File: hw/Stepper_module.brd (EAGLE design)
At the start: 25 x 45 mm, 43 parts, among them J1 GROVE-4P-2.0-3470130P1, J2 GROVE-4P-2.0-3470130P1, X1 22-23-2021, X2 22-23-2041, X4 53047-04, X5 53047-04

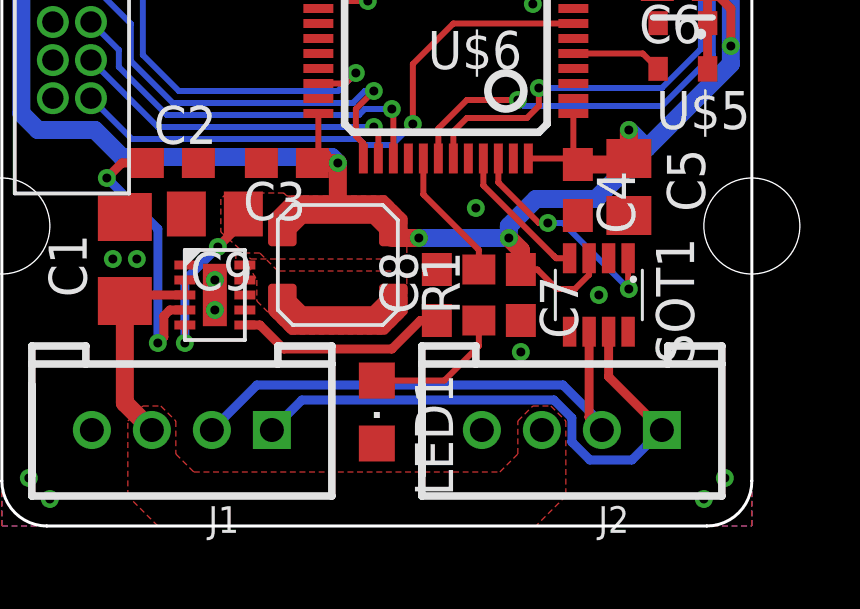
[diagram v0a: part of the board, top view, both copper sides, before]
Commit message: Added bottom silkscreen
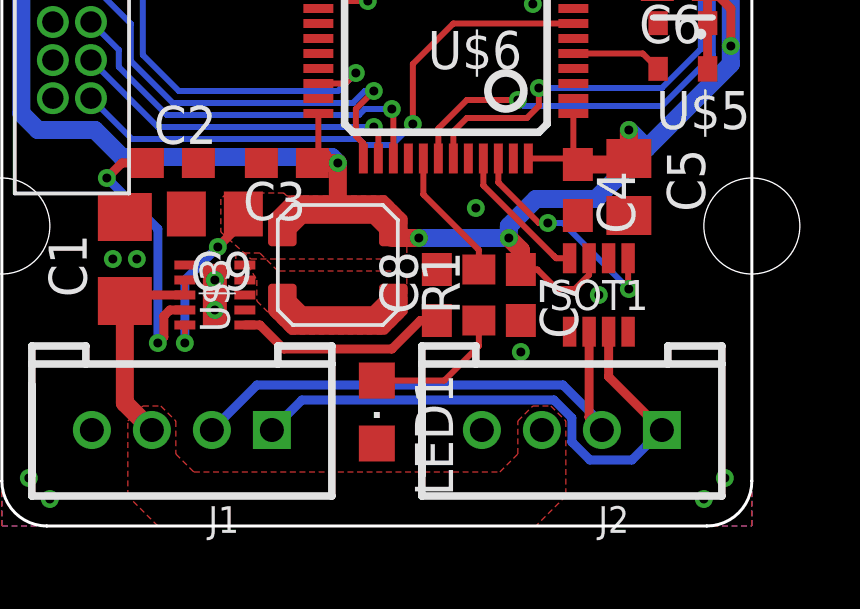
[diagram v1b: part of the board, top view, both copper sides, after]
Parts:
- SOT1: device maxim:SOT23-8L -> r2p_ic:SOT23-8L
- U$3: device maxim:TDFN-10 -> r2p_ic:TDFN-10
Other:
- board text added: "Stepper module v1.0 (2015/02)"
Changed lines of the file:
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@@
 <wire x1="6.55" y1="8.8" x2="7.45" y2="8.8" width="0.2" layer="41"/>
 <wire x1="11.4" y1="22.9" x2="13.2" y2="22.9" width="0.2" layer="41"/>
+<text x="4" y="6" size="1.5" layer="200" rot="MR90">Stepper module
+v1.0 (2015/02)</text>
 </plain>
 <attributes>
@@
 <element name="C8" library="rcl" package="C0603" value="10n" x="14.5" y="7.7" rot="R90"/>
 <element name="C9" library="rcl" package="C0805" value="10uF" x="7.1" y="10.4" rot="R180"/>
-<element name="U$3" library="maxim" package="TDFN-10" value="MAX17501" x="7.1" y="7.7"/>
+<element name="U$3" library="r2p_ic" package="TDFN-10" value="MAX17501" x="7.1" y="7.7"/>
 <element name="J1" library="OPL Eagle Library" package="4P-2.0" value="GROVE-4P-2.0-3470130P1" x="6" y="3.2" rot="R180"/>
 <element name="U$6" library="st" package="LQFP48" value="STM32F303C" x="14.8" y="16.5" rot="R180"/>
-<element name="SOT1" library="maxim" package="SOT23-8L" value="MAX3051EKA" x="19.9" y="7.7" rot="R180"/>
+<element name="SOT1" library="r2p_ic" package="SOT23-8L" value="MAX3051EKA" x="19.9" y="7.7" rot="R180"/>
 <element name="U$1" library="r2p_pcb" package="25X45" value="PCB_25X45" x="0" y="0"/>
 <element name="U$5" library="abracon" package="2.5X2" value="ASD" x="22.7" y="16" rot="R180"/>
@@
 </board>
 </drawing>
+<compatibility>
+<note version="6.3" minversion="6.2.2" severity="warning">
+Since Version 6.2.2 text objects can contain more than one line,
+which will not be processed correctly with this version.
+</note>
+</compatibility>
 </eagle>

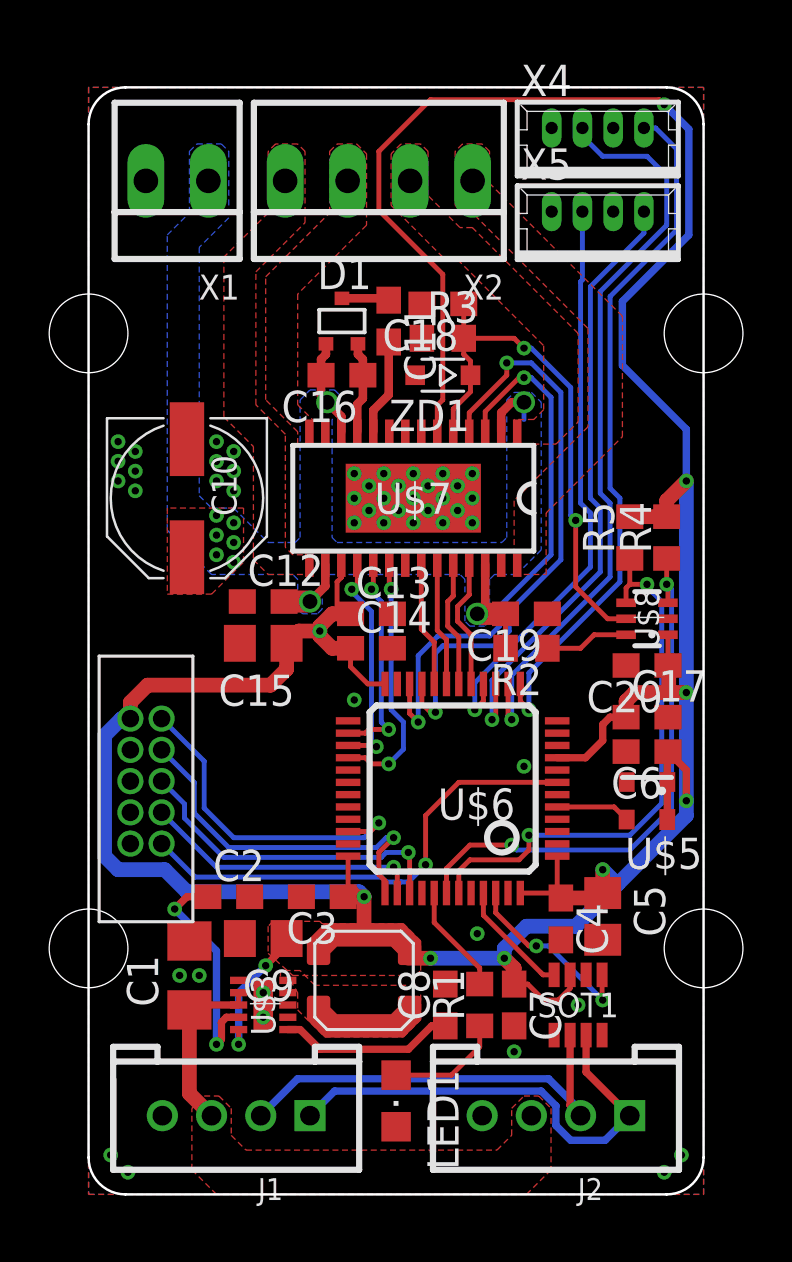
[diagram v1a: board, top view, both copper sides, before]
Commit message: Updated components to R2P Eagle libraries
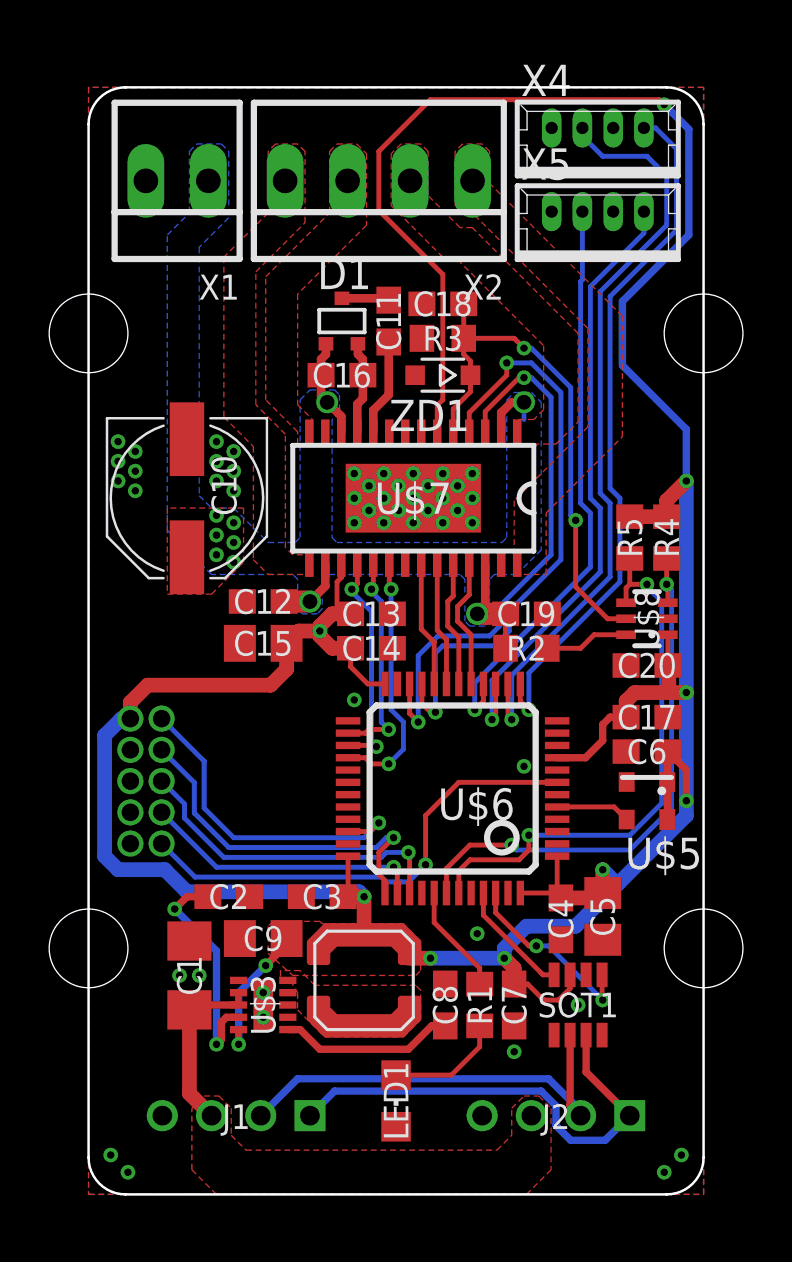
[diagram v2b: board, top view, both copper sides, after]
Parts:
- C1: device rcl:C1206 -> r2p_rcl:C1206
- C11, C12, C13, C14, C16, C17, C18, C19, C2, C20, C3, C4, C6, C7, C8: device rcl:C0603 -> r2p_rcl:C0603
- C15, C5, C9: device rcl:C0805 -> r2p_rcl:C0805
- J1, J2: value GROVE-4P-2.0-3470130P1 -> R2P_BUS-VERTICAL; device OPL Eagle Library:4P-2.0 -> r2p_connector:OPL-EAGLE-LIBRARY_4P-2.0
- LED1: value (none) -> LED0805; device led:CHIPLED_0805 -> r2p_led:CHIPLED_0805
- R1, R2, R3, R4, R5: device rcl:R0603 -> r2p_rcl:R0603
- U$4: value FTSH-105TH -> JTAG-TH; device samtec:FTSH-105-TH -> r2p_connector:SAMTEC_FTSH-105-TH
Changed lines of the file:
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@@
 </class>
 </classes>
-<designrules name="ITead_rule-8mil *">
+<designrules name="2layer_0.2mm">
 <description language="de">&lt;b&gt;EAGLE Design Rules&lt;/b&gt;
 &lt;p&gt;
@@
 </description>
 <param name="layerSetup" value="(1*16)"/>
-<param name="mtCopper" value="0.035mm 0.035mm 0.035mm 0.035mm 0.035mm 0.035mm 0.035mm 0.035mm 0.035mm 0.035mm 0.035mm 0.035mm 0.035mm 0.035mm 0.035mm 0.035mm"/>
-<param name="mtIsolate" value="1.5mm 0.15mm 0.2mm 0.15mm 0.2mm 0.15mm 0.2mm 0.15mm 0.2mm 0.15mm 0.2mm 0.15mm 0.2mm 0.15mm 0.2mm"/>
+<param name="mtCopper" value="0.035mm 0.0175mm 0.035mm 0.035mm 0.035mm 0.035mm 0.035mm 0.035mm 0.035mm 0.035mm 0.035mm 0.035mm 0.035mm 0.035mm 0.0175mm 0.035mm"/>
+<param name="mtIsolate" value="1.5mm 1.1mm 0.2mm 0.15mm 0.2mm 0.15mm 0.2mm 0.15mm 0.2mm 0.15mm 0.2mm 0.15mm 0.2mm 0.15mm 0.2mm"/>
 <param name="mdWireWire" value="0.2mm"/>
 <param name="mdWirePad" value="0.2mm"/>
@@
 <param name="mdViaViaSameLayer" value="8mil"/>
 <param name="mnLayersViaInSmd" value="2"/>
-<param name="mdCopperDimension" value="10mil"/>
-<param name="mdDrill" value="10mil"/>
+<param name="mdCopperDimension" value="0.3mm"/>
+<param name="mdDrill" value="0.3mm"/>
 <param name="mdSmdStop" value="0mil"/>
 <param name="msWidth" value="0.2mm"/>
@@
 <param name="mvStopFrame" value="1"/>
 <param name="mvCreamFrame" value="0"/>
-<param name="mlMinStopFrame" value="2mil"/>
-<param name="mlMaxStopFrame" value="2mil"/>
+<param name="mlMinStopFrame" value="0.05mm"/>
+<param name="mlMaxStopFrame" value="0.05mm"/>
 <param name="mlMinCreamFrame" value="0mil"/>
 <param name="mlMaxCreamFrame" value="0mil"/>
-<param name="mlViaStopLimit" value="100mil"/>
+<param name="mlViaStopLimit" value="2.5mm"/>
 <param name="srRoundness" value="0"/>
 <param name="srMinRoundness" value="0mil"/>
 <param name="srMaxRoundness" value="0mil"/>
-<param name="slThermalIsolate" value="10mil"/>
+<param name="slThermalIsolate" value="0.25mm"/>
 <param name="slThermalsForVias" value="0"/>
 <param name="dpMaxLengthDifference" value="10mm"/>
@@
 </autorouter>
 <elements>
-<element name="C6" library="rcl" package="C0603" value="10n" x="22.7" y="18" rot="R180"/>
-<element name="C17" library="rcl" package="C0603" value="100n" x="22.7" y="19.4"/>
-<element name="C14" library="rcl" package="C0603" value="100n" x="11.5" y="22.2"/>
-<element name="C4" library="rcl" package="C0603" value="100n" x="19.2" y="11.2" rot="R270"/>
-<element name="C5" library="rcl" package="C0805" value="4.7u" x="20.9" y="11.3" rot="R270"/>
-<element name="C3" library="rcl" package="C0603" value="100n" x="9.5" y="12.1" rot="R180"/>
-<element name="C7" library="rcl" package="C0603" value="100n" x="17.3" y="7.7" rot="R270"/>
-<element name="LED1" library="led" package="CHIPLED_0805" value="" x="12.5" y="3.8" rot="R180"/>
-<element name="R1" library="rcl" package="R0603" value="330" x="15.9" y="7.7" rot="R90"/>
-<element name="U$4" library="samtec" package="FTSH-105-TH" value="FTSH-105TH" x="1.7" y="16.8" rot="R270"/>
-<element name="J2" library="OPL Eagle Library" package="4P-2.0" value="GROVE-4P-2.0-3470130P1" x="19" y="3.2" rot="R180"/>
+<element name="C6" library="r2p_rcl" package="C0603" value="10n" x="22.7" y="18" rot="R180"/>
+<element name="C17" library="r2p_rcl" package="C0603" value="100n" x="22.7" y="19.4"/>
+<element name="C14" library="r2p_rcl" package="C0603" value="100n" x="11.5" y="22.2"/>
+<element name="C4" library="r2p_rcl" package="C0603" value="100n" x="19.2" y="11.2" rot="R270"/>
+<element name="C5" library="r2p_rcl" package="C0805" value="4.7u" x="20.9" y="11.3" rot="R270"/>
+<element name="C3" library="r2p_rcl" package="C0603" value="100n" x="9.5" y="12.1" rot="R180"/>
+<element name="C7" library="r2p_rcl" package="C0603" value="100n" x="17.3" y="7.7" rot="R270"/>
+<element name="LED1" library="r2p_led" package="CHIPLED_0805" value="LED0805" x="12.5" y="3.8" rot="R180"/>
+<element name="R1" library="r2p_rcl" package="R0603" value="330" x="15.9" y="7.7" rot="R90"/>
+<element name="U$4" library="r2p_connector" package="SAMTEC_FTSH-105-TH" value="JTAG-TH" x="1.7" y="16.8" rot="R270"/>
+<element name="J2" library="r2p_connector" package="OPL-EAGLE-LIBRARY_4P-2.0" value="R2P_BUS-VERTICAL" x="19" y="3.2" rot="R180"/>
 <element name="U$2" library="coilcraft" package="LPS4018" value="LPS4018" x="11.2" y="8.7" rot="R90"/>
-<element name="C1" library="rcl" package="C1206" value="1u" x="4.1" y="8.9" rot="R90"/>
-<element name="C2" library="rcl" package="C0603" value="1u" x="5.7" y="12.1"/>
-<element name="C8" library="rcl" package="C0603" value="10n" x="14.5" y="7.7" rot="R90"/>
-<element name="C9" library="rcl" package="C0805" value="10uF" x="7.1" y="10.4" rot="R180"/>
+<element name="C1" library="r2p_rcl" package="C1206" value="1u" x="4.1" y="8.9" rot="R90"/>
+<element name="C2" library="r2p_rcl" package="C0603" value="1u" x="5.7" y="12.1"/>
+<element name="C8" library="r2p_rcl" package="C0603" value="10n" x="14.5" y="7.7" rot="R90"/>
+<element name="C9" library="r2p_rcl" package="C0805" value="10uF" x="7.1" y="10.4" rot="R180"/>
 <element name="U$3" library="r2p_ic" package="TDFN-10" value="MAX17501" x="7.1" y="7.7"/>
-<element name="J1" library="OPL Eagle Library" package="4P-2.0" value="GROVE-4P-2.0-3470130P1" x="6" y="3.2" rot="R180"/>
+<element name="J1" library="r2p_connector" package="OPL-EAGLE-LIBRARY_4P-2.0" value="R2P_BUS-VERTICAL" x="6" y="3.2" rot="R180"/>
 <element name="U$6" library="st" package="LQFP48" value="STM32F303C" x="14.8" y="16.5" rot="R180"/>
 <element name="SOT1" library="r2p_ic" package="SOT23-8L" value="MAX3051EKA" x="19.9" y="7.7" rot="R180"/>
@@
 <element name="C10" library="rcl" package="PANASONIC_D" value="" x="4" y="28.3" rot="R270"/>
 <element name="D1" library="nxp" package="SC70" value="BAV99W" x="10.3" y="35.5"/>
-<element name="C11" library="rcl" package="C0603" value="100n" x="12.2" y="35.5" rot="R270"/>
-<element name="C13" library="rcl" package="C0603" value="100n" x="11.5" y="23.6"/>
-<element name="C15" library="rcl" package="C0805" value="10u" x="7.1" y="22.4" rot="R180"/>
+<element name="C11" library="r2p_rcl" package="C0603" value="100n" x="12.2" y="35.5" rot="R270"/>
+<element name="C13" library="r2p_rcl" package="C0603" value="100n" x="11.5" y="23.6"/>
+<element name="C15" library="r2p_rcl" package="C0805" value="10u" x="7.1" y="22.4" rot="R180"/>
 <element name="U$8" library="microchip" package="SC70-6L" value="MCP4017" x="22.7" y="23.4" rot="R90"/>
-<element name="R2" library="rcl" package="R0603" value="330" x="17.8" y="22.2" rot="R180"/>
-<element name="R3" library="rcl" package="R0603" value="330" x="14.4" y="34.8"/>
-<element name="C16" library="rcl" package="C0603" value="100n" x="10.3" y="33.3" rot="R180"/>
-<element name="C18" library="rcl" package="C0603" value="100n" x="14.4" y="36.2" rot="R180"/>
+<element name="R2" library="r2p_rcl" package="R0603" value="330" x="17.8" y="22.2" rot="R180"/>
+<element name="R3" library="r2p_rcl" package="R0603" value="330" x="14.4" y="34.8"/>
+<element name="C16" library="r2p_rcl" package="C0603" value="100n" x="10.3" y="33.3" rot="R180"/>
+<element name="C18" library="r2p_rcl" package="C0603" value="100n" x="14.4" y="36.2" rot="R180"/>
 <element name="ZD1" library="dp_devices" package="SOD-323F" value="" x="14.4" y="33.3" rot="R180"/>
-<element name="R4" library="rcl" package="R0603" value="4k7" x="23.5" y="26.7" rot="R90"/>
-<element name="R5" library="rcl" package="R0603" value="4k7" x="22" y="26.7" rot="R90"/>
-<element name="C12" library="rcl" package="C0603" value="100n" x="7.1" y="24.1"/>
-<element name="C19" library="rcl" package="C0603" value="100n" x="17.8" y="23.6" rot="R180"/>
+<element name="R4" library="r2p_rcl" package="R0603" value="4k7" x="23.5" y="26.7" rot="R90"/>
+<element name="R5" library="r2p_rcl" package="R0603" value="4k7" x="22" y="26.7" rot="R90"/>
+<element name="C12" library="r2p_rcl" package="C0603" value="100n" x="7.1" y="24.1"/>
+<element name="C19" library="r2p_rcl" package="C0603" value="100n" x="17.8" y="23.6" rot="R180"/>
 <element name="X4" library="con-molex" package="53047-04" value="53047-04" x="20.7" y="42.9">
 <attribute name="OC_NEWARK" value="38C9900" x="20.7" y="42.9" size="1.778" layer="27" display="off"/>
@@
 <attribute name="OC_FARNELL" value="9733060" x="20.7" y="39.5" size="1.778" layer="27" display="off"/>
 </element>
-<element name="C20" library="rcl" package="C0603" value="100n" x="22.7" y="21.5" rot="R180"/>
+<element name="C20" library="r2p_rcl" package="C0603" value="100n" x="22.7" y="21.5" rot="R180"/>
 </elements>
 <signals>
